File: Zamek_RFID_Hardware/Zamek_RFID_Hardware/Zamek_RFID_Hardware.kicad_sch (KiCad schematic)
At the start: 10 parts, among them J1 Conn_01x08, J2 Conn_01x08, J3 Conn_01x04, J4 Conn_01x03

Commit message: przydzielanie footprintów
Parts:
- D1, D2: footprint (none) -> LED_THT:LED_D5.0mm
- R1, R2: footprint (none) -> Resistor_THT:R_Axial_DIN0207_L6.3mm_D2.5mm_P10.16mm_Horizontal
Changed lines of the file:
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@@
 			)
 		)
-		(property "Footprint" ""
+		(property "Footprint" "LED_THT:LED_D5.0mm"
 			(at 241.3 73.66 0)
 			(hide yes)
@@
 			)
 		)
-		(property "Footprint" ""
+		(property "Footprint" "Resistor_THT:R_Axial_DIN0207_L6.3mm_D2.5mm_P10.16mm_Horizontal"
 			(at 229.362 76.2 90)
 			(hide yes)
@@
 			)
 		)
-		(property "Footprint" ""
+		(property "Footprint" "LED_THT:LED_D5.0mm"
 			(at 241.3 95.25 0)
 			(hide yes)
@@
 			)
 		)
-		(property "Footprint" ""
+		(property "Footprint" "Resistor_THT:R_Axial_DIN0207_L6.3mm_D2.5mm_P10.16mm_Horizontal"
 			(at 229.362 95.25 90)
 			(hide yes)

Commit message: Projekt PCB: Ułożenie elementów i narysowanie krawędzi płytki (Widok 3D)
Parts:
- BZ1: footprint (none) -> Buzzer_Beeper:Buzzer_12x9.5RM7.6
- J1, J2: footprint (none) -> Connector_PinHeader_2.54mm:PinHeader_1x08_P2.54mm_Vertical
- J3: footprint (none) -> Connector_PinHeader_2.54mm:PinHeader_1x04_P2.54mm_Vertical
- J4: footprint (none) -> Connector_PinHeader_2.54mm:PinHeader_1x03_P2.54mm_Vertical
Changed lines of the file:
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@@
 			)
 		)
-		(property "Footprint" ""
+		(property "Footprint" "Buzzer_Beeper:Buzzer_12x9.5RM7.6"
 			(at 236.855 114.3 90)
 			(hide yes)
@@
 			)
 		)
-		(property "Footprint" ""
+		(property "Footprint" "Connector_PinHeader_2.54mm:PinHeader_1x08_P2.54mm_Vertical"
 			(at 119.38 91.44 0)
 			(hide yes)
@@
 			)
 		)
-		(property "Footprint" ""
+		(property "Footprint" "Connector_PinHeader_2.54mm:PinHeader_1x04_P2.54mm_Vertical"
 			(at 191.77 109.22 0)
 			(hide yes)
@@
 			)
 		)
-		(property "Footprint" ""
+		(property "Footprint" "Connector_PinHeader_2.54mm:PinHeader_1x03_P2.54mm_Vertical"
 			(at 234.95 138.43 0)
 			(hide yes)
@@
 			)
 		)
-		(property "Footprint" ""
+		(property "Footprint" "Connector_PinHeader_2.54mm:PinHeader_1x08_P2.54mm_Vertical"
 			(at 191.77 88.9 0)
 			(hide yes)

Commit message: poprawki i wylewka
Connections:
- net +3.3V: no longer A1.4 (GND), BZ1.2 (-), D1.2 (A), D2.2 (A), J1.3 (Pin_3), J3.1 (Pin_1), J4.2 (Pin_2)
- net GND: now reaches A1.29 (GND)
- net GND: now also A1.4 (GND), BZ1.2 (-), D1.2 (A), D2.2 (A), J1.3 (Pin_3), J3.1 (Pin_1), J4.2 (Pin_2)

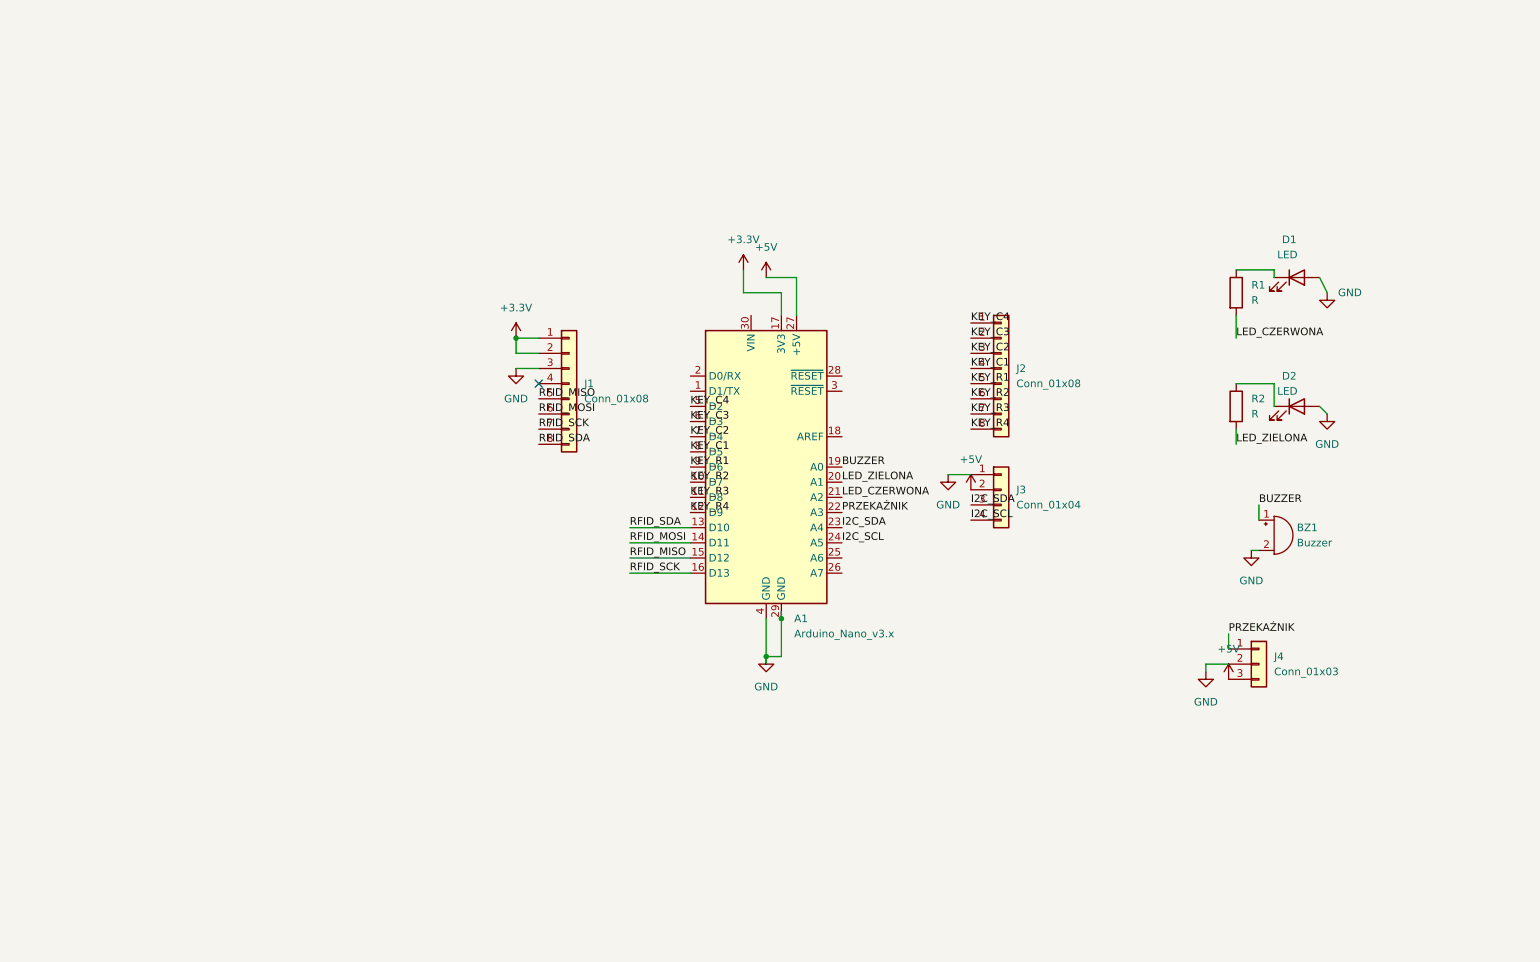
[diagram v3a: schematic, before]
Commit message: hw: schematic v1.1 - fix LED polarity, add decoupling, SPI level shifting and buzzer driver
- Rotate D1/D2 so the GPIO drives the anode through the resistor;
  PCB footprints rotated 180 deg in place, existing copper reused
- R1 = 300 R, R2 = 200 R (10 mA per LED)
- Add 100 uF + 100 nF on +5V at the relay connector and
  10 uF + 100 nF on +3.3V at the RC522 connector
- Add 1k/2k dividers on SS, MOSI and SCK: MFRC522 inputs are limited
  to VDD + 0.5 V; MISO stays direct (3.3 V is above ATmega328P VIH)
- Drive the buzzer through a BC547 with a 1N4148 flyback diode
- Add test points on +5V, +3.3V and GND, and four M3 mounting holes
- Rename net PRZEKAZNIK to RELAY (ASCII only for CAM tools)
- ERC clean: no-connect flags on unused Nano pins, PWR_FLAG on GND

PCB layout not yet updated from the schematic.
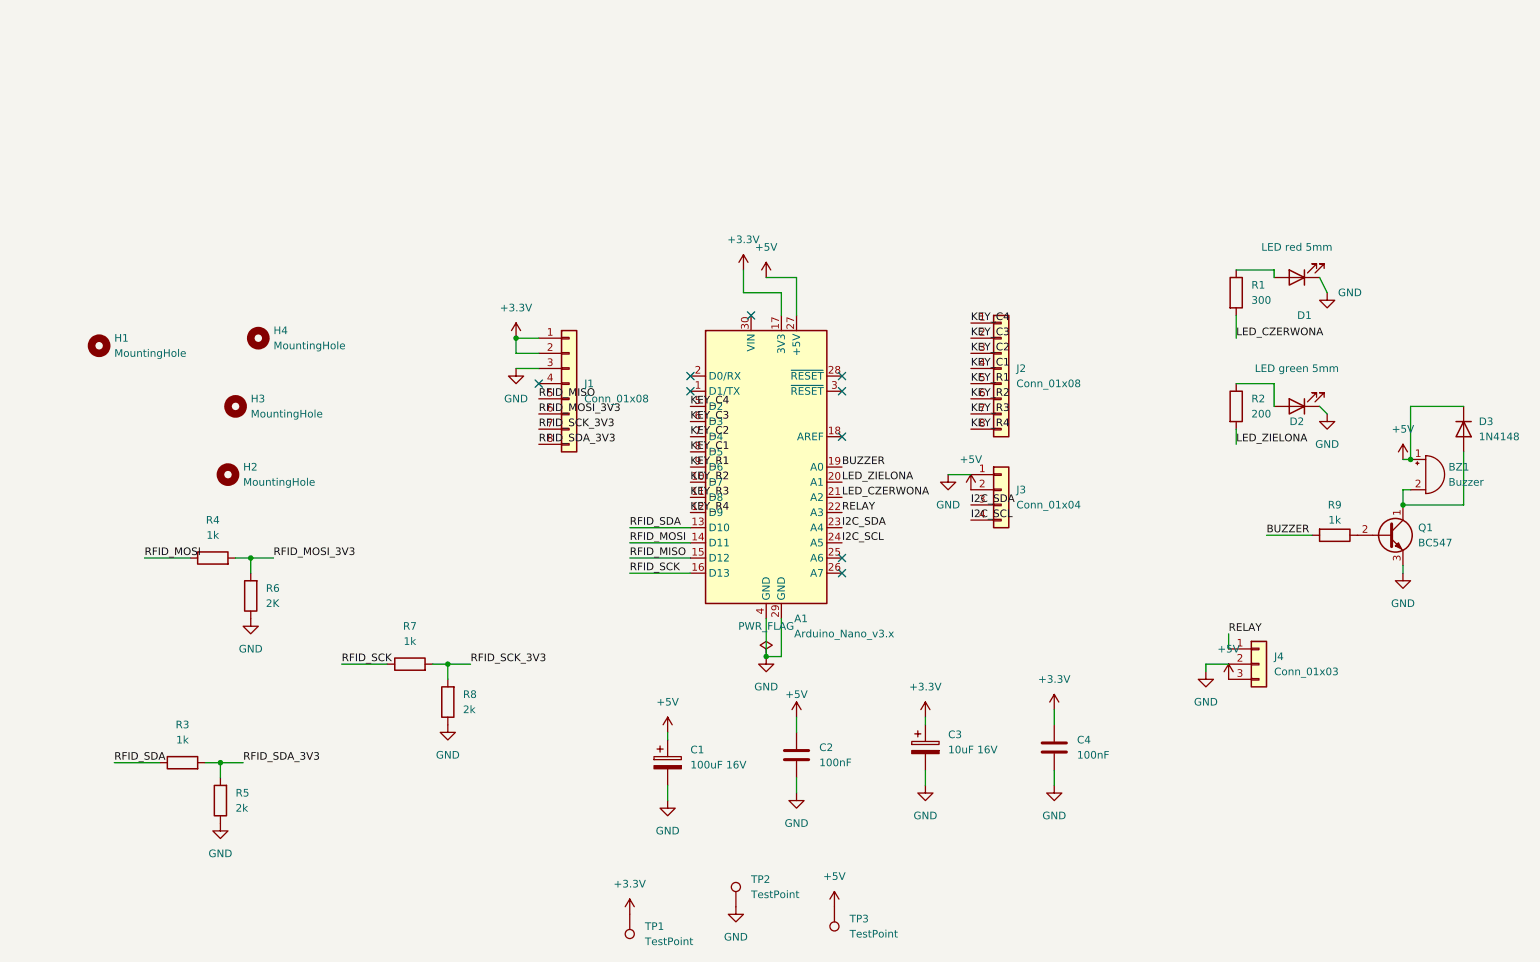
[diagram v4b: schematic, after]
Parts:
- added C1: 100uF 16V, Capacitor_THT:CP_Radial_D6.3mm_P2.50mm, symbol Device:C_Polarized
- added C2, C4: 100nF, Capacitor_THT:C_Disc_D5.0mm_W2.5mm_P5.00mm, symbol Device:C
- added C3: 10uF 16V, Capacitor_THT:CP_Radial_D5.0mm_P2.00mm, symbol Device:C_Polarized
- added D3: 1N4148, Diode_THT:D_DO-35_SOD27_P7.62mm_Horizontal, symbol Diode:1N4148
- added H1, H2, H3, H4: MountingHole, MountingHole:MountingHole_3.2mm_M3, symbol Mechanical:MountingHole
- added Q1: BC547, Package_TO_SOT_THT:TO-92_Inline, symbol Transistor_BJT:BC547
- added R3, R4, R7, R9: 1k, Resistor_THT:R_Axial_DIN0207_L6.3mm_D2.5mm_P10.16mm_Horizontal, symbol Device:R
- added R5, R8: 2k, Resistor_THT:R_Axial_DIN0207_L6.3mm_D2.5mm_P10.16mm_Horizontal, symbol Device:R
- added R6: 2K, Resistor_THT:R_Axial_DIN0207_L6.3mm_D2.5mm_P10.16mm_Horizontal, symbol Device:R
- added TP1, TP2, TP3: TestPoint, TestPoint:TestPoint_THTPad_D2.0mm_Drill1.0mm, symbol Connector:TestPoint
- D1: value LED -> LED red 5mm
- D2: value LED -> LED green 5mm
- R1: value R -> 300
- R2: value R -> 200
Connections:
- net +3.3V: now also C3.1, C4.1, TP1.1
- net +5V: now also BZ1.1 (+), C1.1, C2.1, D3.1 (K), TP3.1
- net BUZZER: now also R9.2; no longer BZ1.1 (+)
- net GND: now also D1.1 (K), D2.1 (K), C1.2, C2.2, C3.2, C4.2, Q1.3 (E), R5.1, R6.1, R8.1, TP2.1; no longer BZ1.2 (-), D1.2 (A), D2.2 (A)
- net RFID_MOSI: now also R4.1; no longer J1.6 (Pin_6)
- net RFID_SCK: now also R7.1; no longer J1.7 (Pin_7)
- net RFID_SDA: now also R3.1; no longer J1.8 (Pin_8)
- net at R1.1: now also D1.2 (A); no longer D1.1 (K)
- net at R2.1: now also D2.2 (A); no longer D2.1 (K)
- net PRZEKAŹNIK renamed RELAY
- new net: BZ1.2 (-), D3.2 (A), Q1.1 (C)
- new net: Q1.2 (B), R9.1
- new net RFID_MOSI_3V3: J1.6 (Pin_6), R4.2, R6.2
- new net RFID_SCK_3V3: J1.7 (Pin_7), R7.2, R8.2
- new net RFID_SDA_3V3: J1.8 (Pin_8), R3.2, R5.2
- no-connect marks 1 -> 9
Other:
- moved on the sheet: BZ1, D1, D2

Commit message: hw: fix R6 value notation (2K - 2k)
- consistent with R5/R8, so BOM groups all 2k resistors in one line
- lowercase k is the SI prefix
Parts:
- R6: value 2K -> 2k
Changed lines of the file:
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@@
 			)
 		)
-		(property "Value" "2K"
+		(property "Value" "2k"
 			(at 68.58 128.2699 0)
 			(show_name no)

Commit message: hw: exclude test points from BOM
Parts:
- TP1, TP2, TP3: now left out of the parts list
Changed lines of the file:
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@@
 		(body_style 1)
 		(exclude_from_sim no)
-		(in_bom yes)
+		(in_bom no)
 		(on_board yes)
 		(in_pos_files yes)
@@
 		(body_style 1)
 		(exclude_from_sim no)
-		(in_bom yes)
+		(in_bom no)
 		(on_board yes)
 		(in_pos_files yes)
@@
 		(body_style 1)
 		(exclude_from_sim no)
-		(in_bom yes)
-		(on_board yes)
-		(in_pos_files yes)
+		(in_bom no)
+		(on_board yes)
+		(in_pos_files yes)

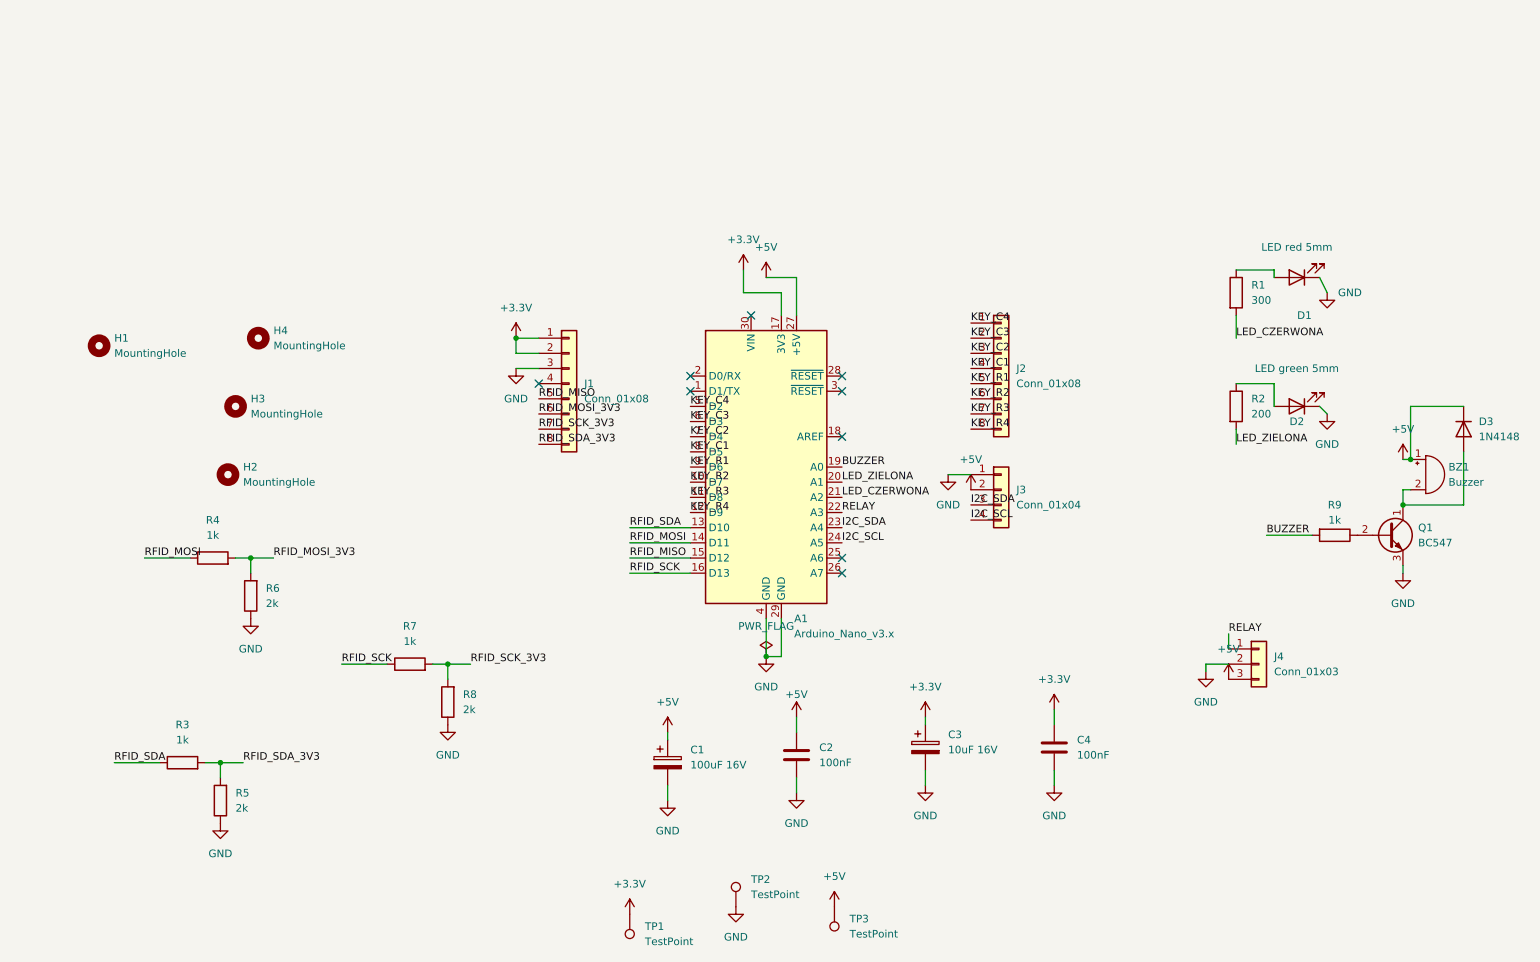
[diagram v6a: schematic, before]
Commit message: hw: set R2 to 300 ohm, tidy up schematic labels and title block
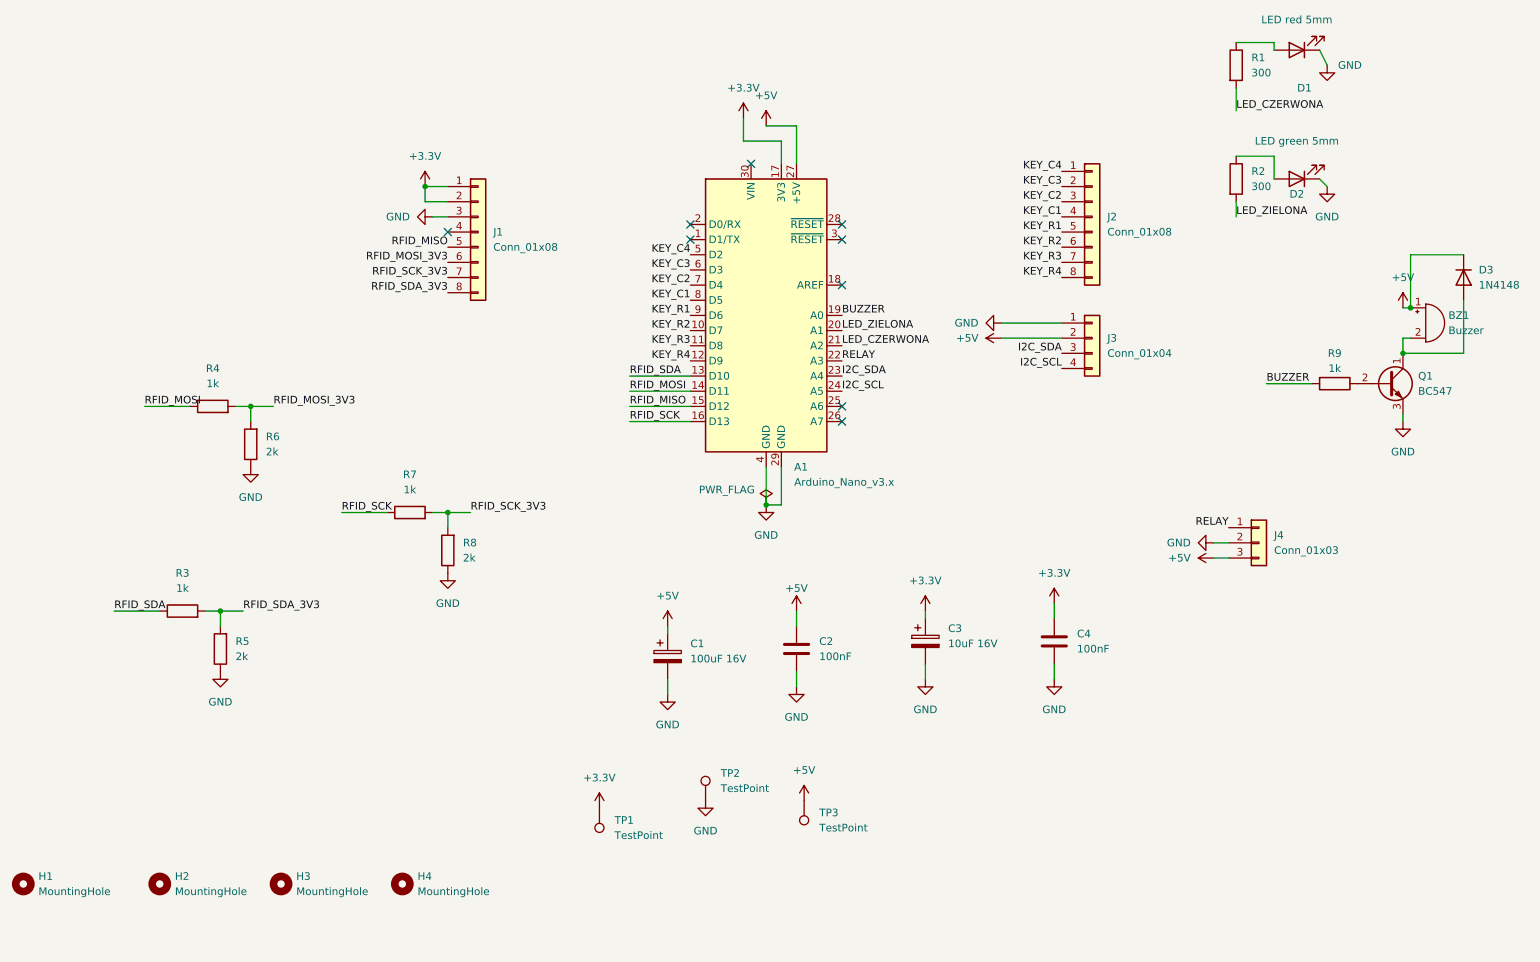
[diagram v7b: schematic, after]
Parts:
- R2: value 200 -> 300
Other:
- company: (none) -> Łukasz Jęśko
- title: (none) -> Smart Access Control
- moved on the sheet: A1, BZ1, C1, C2, C3, C4, D1, D2, D3, H1, H2, H3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
